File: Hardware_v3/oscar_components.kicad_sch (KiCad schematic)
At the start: 65 parts, among them J1 SWD_Header, J10 USB_C_Receptacle, J11 MIDI_OUT, J2 ChannelA_In, J3 ChannelB_In, J4 ChannelC_In, J5 ChA_Buff_Out, J6 ChB_Buff_Out, J7 ChC_Buff_Out, J8 MIDI_IN, J9 Eurorack_10_pin_power, SW1 Left_Encoder, SW2 Right_Encoder, SW3 Reset_Button, SW4 Menu_Button, U1 STM32F446RETx, U2 ILI9341_SPI_Daughterboard, U3 MCP6004, U4 TL074, U5 LT1117-3.3, U6 6N137, Y1 8MHz

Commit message: Folder reorganisation
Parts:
- J11: value MIDI_OUT -> MIDI_THROUGH
- Y1: footprint Crystal:Crystal_SMD_Abracon_ABM3-2Pin_5.0x3.2mm -> Custom_Footprints:Crystal_SMD_5032-2Pin_5.0x3.2mm_Large_Pads
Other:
- note added: "Buttons"
- note added: "Connectors"
- note added: "Encoders"
- note added: "Illuminated Buttons"
- note added: "Input and Buffers"
- note added: "MIDI"
- note added: "Microcontroller"
- note added: "Power Supply"
- note added: "USB"
- note removed: "Fixes for next version: Pull-down on BOOT0 pin Move daughterboard components to main board MIDI in using TRS Opto-coupler on MIDI MIDI buffered through (x2?) Buffered mults on ABC channels Remove cap on encoder button Decoupling caps on MCU and Op-amps R2 on daughterboard increased to 1.5k to improve backlight brightness? Oscillator load capacitors"
- company: (none) -> Mountjoy Modular
- title: (none) -> Oscar
- moved on the sheet: BTN1, BTN2, BTN3, C1, C11, C12, C14, C16, C4, C6, C7, C8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

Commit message: PCB Layout
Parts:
- added TP1, TP2, TP3, TP4, TP5: TestPoint, Custom_Footprints:1.3mm_Test_Point, symbol Connector:TestPoint
- renumbered C8 to C1, C6 to C10, C16 to C11, C7 to C12, C10 to C14, C11 to C15, C12 to C2, C1 to C3, C2 to C4, C3 to C5, C4 to C6, C9 to C7, C14 to C8, C5 to C9, D4 to D3, D3 to D4, J11 to J10, J10 to J11, J9 to J2, J4 to J3, J2 to J4, J3 to J5, J7 to J6, J5 to J7, J6 to J8, J8 to J9, R13 to R1, R9 to R10, R16 to R11, R17 to R12, R10 to R13, R11 to R14, R12 to R15, R14 to R16, R15 to R17, R1 to R2, R2 to R3, R3 to R4, R4 to R5, R5 to R6, R6 to R7, R7 to R8, R8 to R9, SW3 to SW1, SW4 to SW2, SW1 to SW3, SW2 to SW4, U5 to U1, U1 to U3, U3 to U5
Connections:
- net +12V: now also TP1.1
- net +3.3V: now also TP5.1
- net -12V: now also TP2.1
- net GND: now also TP3.1, TP4.1
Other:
- note removed: "Illuminated Buttons"
- moved on the sheet: BTN1, BTN2, BTN3, C1, C10, C12, C13, C14, C3, C4, C5, C6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

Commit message: Started working on panel
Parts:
- added J12: Debug, Connector_PinHeader_2.54mm:PinHeader_1x03_P2.54mm_Vertical, symbol Connector:Conn_01x03_Pin
- SW1: footprint Button_Switch_THT:SW_PUSH_6mm -> Custom_Footprints:SW_PUSH_6mm_aligned
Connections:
- net GND: now also J12.3 (Pin_3)
- net DEBUG1: now reaches U3.51 (PC10)
- net DEBUG1: now also J12.1 (Pin_1)
- net DEBUG2: now reaches U3.52 (PC11)
- net DEBUG2: now also J12.2 (Pin_2)
- no-connect marks 43 -> 41
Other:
- note added: "UART4_RX"
- moved on the sheet: TP1, TP2, TP3, TP4, TP5

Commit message: Control Layout change
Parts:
- SW2: footprint Button_Switch_THT:SW_PUSH_6mm -> Custom_Footprints:SW_PUSH_6mm_aligned
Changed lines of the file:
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@@
 			)
 		)
-		(property "Footprint" "Button_Switch_THT:SW_PUSH_6mm"
+		(property "Footprint" "Custom_Footprints:SW_PUSH_6mm_aligned"
 			(at 194.31 29.21 0)
 			(effects

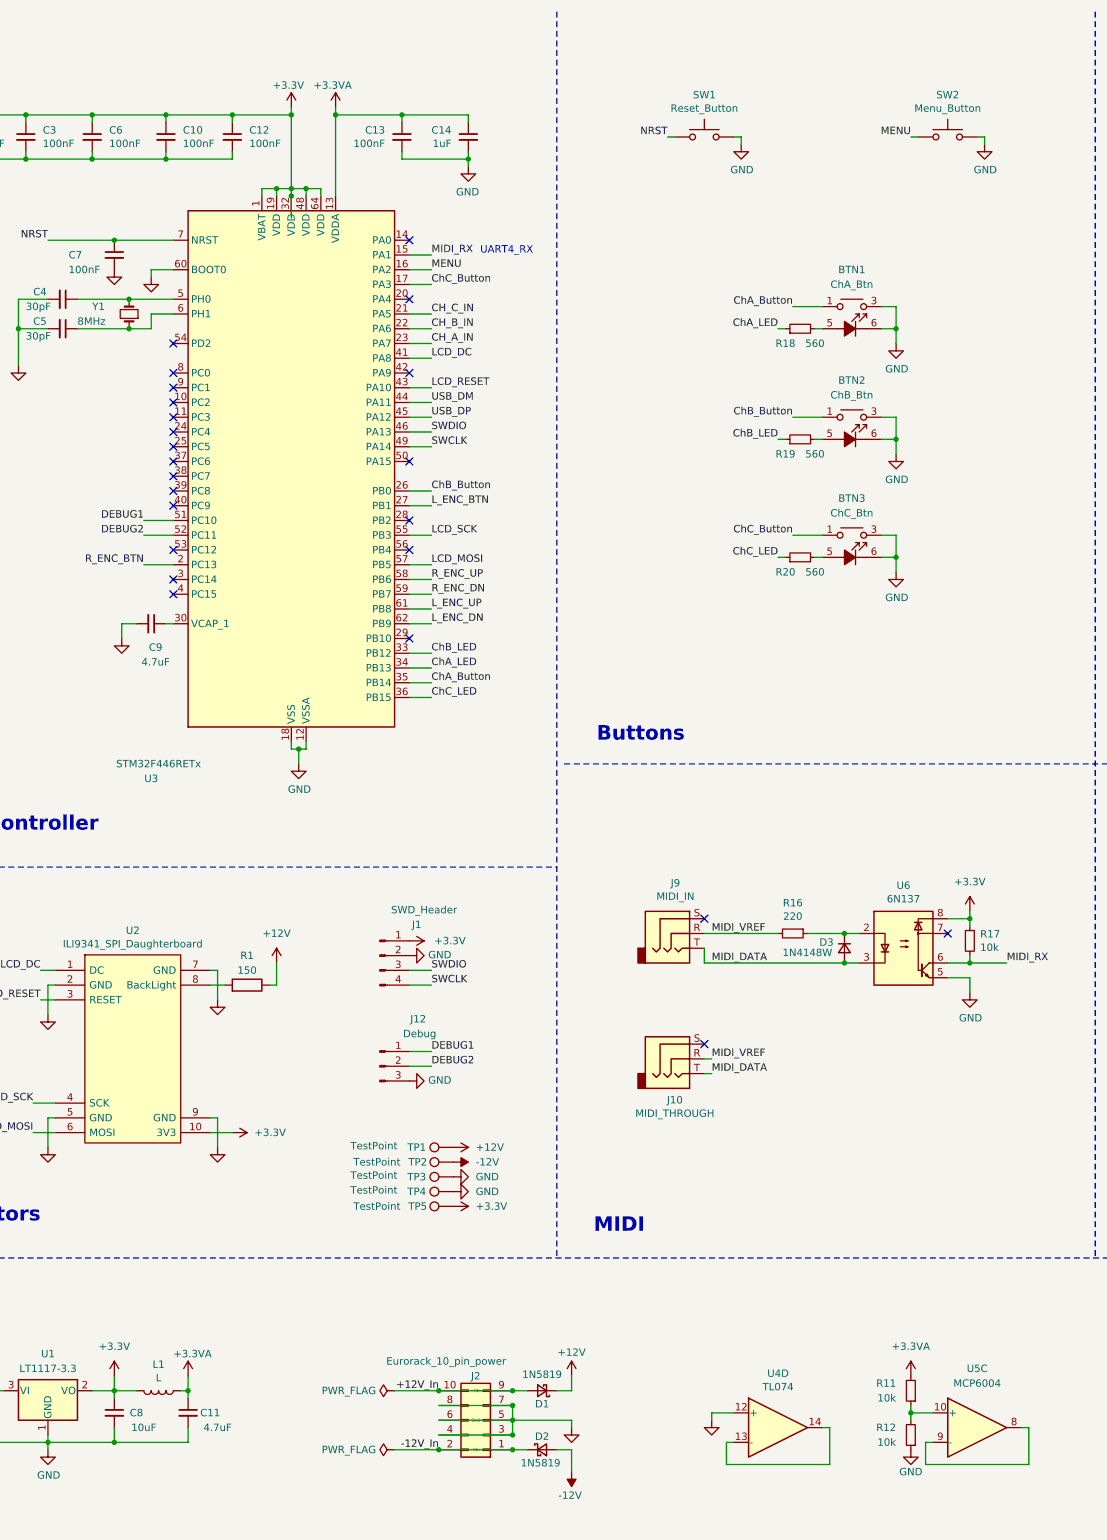
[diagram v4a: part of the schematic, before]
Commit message: Started adding JLC part numbers; changed optocoupler to H11L1
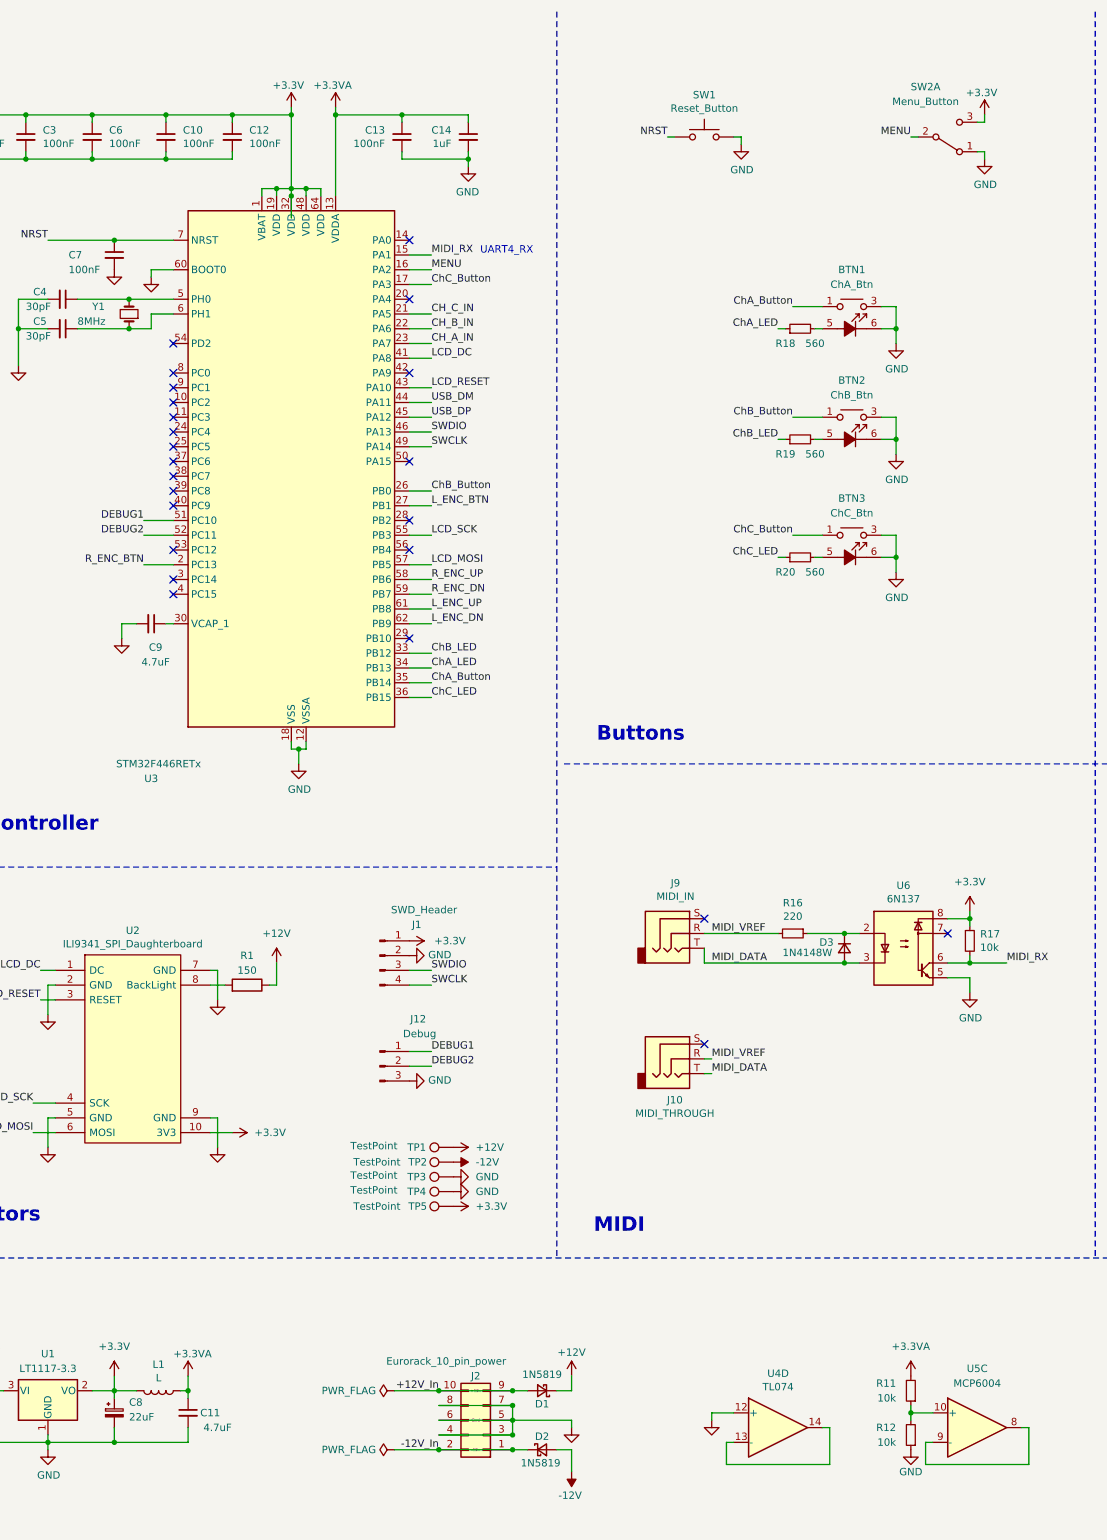
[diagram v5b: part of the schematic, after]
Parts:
- removed C8: 10uF, Capacitor_SMD:CP_Elec_4x5.8, symbol Device:C_Small
- added C8: 22uF, Capacitor_SMD:CP_Elec_4x5.8, symbol Device:C_Polarized_Small
- SW2: footprint Custom_Footprints:SW_PUSH_6mm_aligned -> Custom_Footprints:Low-Profile_Push_Button; symbol Switch:SW_Push -> Low-Profile Push Button:Low-Profile_Push_Button
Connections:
- net +3.3V: now also SW2.3 (C), C8.1
- net GND: now also SW2.1 (A), C8.2; no longer SW2.2
- net MENU: now also SW2.2 (B); no longer SW2.1
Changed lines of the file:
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@@
 	(wire
 		(pts
-			(xy 200.66 34.29) (xy 200.66 35.56)
+			(xy 200.66 36.83) (xy 200.66 38.1)
 		)
 		(stroke
@@
 	(wire
 		(pts
+			(xy 200.66 30.48) (xy 200.66 31.75)
+		)
+		(stroke
+			(width 0)
+			(type default)
+		)
+	)
+	(wire
+		(pts
 			(xy 187.96 252.73) (xy 187.96 254)
 		)
@@
 	(wire
 		(pts
+			(xy 200.66 31.75) (xy 199.39 31.75)
+		)
+		(stroke
+			(width 0)
+			(type default)
+		)
+	)
+	(wire
+		(pts
 			(xy 365.76 92.71) (xy 365.76 83.82)
 		)
@@
 	(wire
 		(pts
-			(xy 200.66 34.29) (xy 199.39 34.29)
+			(xy 200.66 36.83) (xy 199.39 36.83)
 		)
 		(stroke
@@
 	)
 	(symbol
-		(lib_id "Device:C_Small")
-		(at 50.8 254 0)
-		(unit 1)
-		(exclude_from_sim no)
-		(in_bom yes)
-		(on_board yes)
-		(dnp no)
-		(property "Reference" "C8"
-			(at 54.61 254 0)
-			(effects
-				(font
-					(size 1.27 1.27)
-				)
-			)
-		)
-		(property "Value" "10uF"
-			(at 55.88 256.54 0)
-			(effects
-				(font
-					(size 1.27 1.27)
-				)
-			)
-		)
-		(property "Footprint" "Capacitor_SMD:CP_Elec_4x5.8"
-			(at 50.8 254 0)
-			(effects
-				(font
-					(size 1.27 1.27)
-				)
-				(hide yes)
-			)
-		)
-		(property "Datasheet" "~"
-			(at 50.8 254 0)
-			(effects
-				(font
-					(size 1.27 1.27)
-				)
-				(hide yes)
-			)
-		)
-		(property "Description" "Unpolarized capacitor, small symbol"
-			(at 50.8 254 0)
-			(effects
-				(font
-					(size 1.27 1.27)
-				)
-				(hide yes)
-			)
-		)
-		(pin "1"
-		)
-		(pin "2"
-		)
-		(instances
-			(project ""
-				(path "/258e4395-9768-4091-8bcd-6165e2841a11"
-					(reference "C8")
-					(unit 1)
-				)
-			)
-		)
-	)
-	(symbol
 		(lib_id "Device:L")
 		(at 58.42 250.19 270)
@@
 	(symbol
 		(lib_id "power:GND")
-		(at 200.66 35.56 0)
+		(at 200.66 38.1 0)
 		(unit 1)
 		(exclude_from_sim no)
@@
 		(dnp no)
 		(property "Reference" "#PWR058"
-			(at 200.66 41.91 0)
+			(at 200.66 44.45 0)
 			(effects
 				(font
@@
 		)
 		(property "Value" "GND"
-			(at 200.787 39.9542 0)
+			(at 200.787 42.4942 0)
 			(effects
 				(font
@@
 		)
 		(property "Footprint" ""
-			(at 200.66 35.56 0)
+			(at 200.66 38.1 0)
 			(effects
 				(font
@@
 		)
 		(property "Datasheet" ""
-			(at 200.66 35.56 0)
+			(at 200.66 38.1 0)
 			(effects
 				(font
@@
 		)
 		(property "Description" "Power symbol creates a global label with name \"GND\" , ground"
-			(at 200.66 35.56 0)
+			(at 200.66 38.1 0)
 			(effects
 				(font
@@
 	)
 	(symbol
+		(lib_id "power:+3.3V")
+		(at 200.66 30.48 0)
+		(unit 1)
+		(exclude_from_sim no)
+		(in_bom yes)
+		(on_board yes)
+		(dnp no)
+		(property "Reference" "#PWR068"
+			(at 200.66 34.29 0)
+			(effects
+				(font
+					(size 1.27 1.27)
+				)
+				(hide yes)
+			)
+		)
+		(property "Value" "+3.3V"
+			(at 200.152 26.67 0)
+			(effects
+				(font
+					(size 1.27 1.27)
+				)
+			)
+		)
+		(property "Footprint" ""
+			(at 200.66 30.48 0)
+			(effects
+				(font
+					(size 1.27 1.27)
+				)
+				(hide yes)
+			)
+		)
+		(property "Datasheet" ""
+			(at 200.66 30.48 0)
+			(effects
+				(font
+					(size 1.27 1.27)
+				)
+				(hide yes)
+			)
+		)
+		(property "Description" "Power symbol creates a global label with name \"+3.3V\""
+			(at 200.66 30.48 0)
+			(effects
+				(font
+					(size 1.27 1.27)
+				)
+				(hide yes)
+			)
+		)
+		(pin "1"
+		)
+		(instances
+			(project "oscar_components"
+				(path "/258e4395-9768-4091-8bcd-6165e2841a11"
+					(reference "#PWR068")
+					(unit 1)
+				)
+			)
+		)
+	)
+	(symbol
 		(lib_id "power:GND")
 		(at 187.96 260.35 0)
@@
 	)
 	(symbol
-		(lib_id "Switch:SW_Push")
+		(lib_id "Low-Profile Push Button:Low-Profile_Push_Button")
 		(at 194.31 34.29 0)
+		(mirror x)
 		(unit 1)
 		(exclude_from_sim no)
@@
 		(dnp no)
 		(property "Reference" "SW2"
-			(at 194.31 27.051 0)
+			(at 190.5 25.654 0)
 			(effects
 				(font
@@
 		)
 		(property "Value" "Menu_Button"
-			(at 194.31 29.3624 0)
+			(at 190.5 28.194 0)
 			(effects
 				(font
@@
 			)
 		)
-		(property "Footprint" "Custom_Footprints:SW_PUSH_6mm_aligned"
-			(at 194.31 29.21 0)
+		(property "Footprint" "Custom_Footprints:Low-Profile_Push_Button"
+			(at 194.31 34.29 0)
 			(effects
 				(font
@@
 		)
 		(property "Datasheet" "~"
-			(at 194.31 29.21 0)
+			(at 194.31 34.29 0)
 			(effects
 				(font
@@
 			)
 		)
-		(property "Description" "Push button switch, generic, two pins"
+		(property "Description" "Switch, single pole double throw"
 			(at 194.31 34.29 0)
 			(effects
@@
 		(pin "2"
 		)
+		(pin "3"
+		)
+		(pin "6"
+		)
+		(pin "4"
+		)
+		(pin "5"
+		)
 		(instances
 			(project "oscar_components"
@@
 					(unit 1)
 				)
+			)
+		)
+	)
+	(symbol
+		(lib_id "Device:C_Polarized_Small")
+		(at 50.8 254 0)
+		(unit 1)
+		(exclude_from_sim no)
+		(in_bom yes)
+		(on_board yes)
+		(dnp no)
+		(fields_autoplaced yes)
+		(property "Reference" "C8"
+			(at 53.34 252.1838 0)
+			(effects
+				(font
+					(size 1.27 1.27)
+				)
+				(justify left)
+			)
+		)
+		(property "Value" "22uF"
+			(at 53.34 254.7238 0)
+			(effects
+				(font
+					(size 1.27 1.27)
+				)
+				(justify left)
+			)
+		)
+		(property "Footprint" "Capacitor_SMD:CP_Elec_4x5.8"
+			(at 50.8 254 0)
+			(effects
+				(font
+					(size 1.27 1.27)
+				)
+				(hide yes)
+			)
+		)
+		(property "Datasheet" "~"
+			(at 50.8 254 0)
+			(effects
+				(font
+					(size 1.27 1.27)
+				)
+				(hide yes)
+			)
+		)
+		(property "Description" "Polarized capacitor, small symbol"
+			(at 50.8 254 0)
+			(effects
+				(font
+					(size 1.27 1.27)
+				)
+				(hide yes)
+			)
+		)
+		(pin "1"
+		)
+		(pin "2"
+		)
+		(instances
+			(project "oscar_components"
+				(path "/258e4395-9768-4091-8bcd-6165e2841a11"
+					(reference "C8")
+					(unit 1)
+				)

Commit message: More layout
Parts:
- removed SW2: Menu_Button, Custom_Footprints:Low-Profile_Push_Button, symbol Low-Profile Push Button:Low-Profile_Push_Button
- removed U6: 6N137, Package_DIP:DIP-8_W8.89mm_SMDSocket_LongPads, symbol 6N137:6N137
- added SW2: Menu_Button, Custom_Footprints:SW_PUSH_6mm_aligned, symbol Switch:SW_Push
- added U6: H11L1, Custom_Footprints:H11L1, symbol Isolator:H11L1
- BTN1, BTN2, BTN3: symbol LED_Button_KS01-BLV:KS01-BLV -> Low_Profile_LED_Button:Low_Profile_LED_Button
- R17: value 10k -> 470
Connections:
- net +3.3V: now also U6.6
- net GND: now also SW2.2, U6.5
- net MENU: now also SW2.1
- net MIDI_DATA: now also U6.2
- net MIDI_RX: now also U6.4
- net at D3.1 (K), R16.1: now also U6.1
- no-connect marks 41 -> 40
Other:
- moved on the sheet: C1, C10, C12, C13, C14, C3, C4, C5, C6, C7, C9, J3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
